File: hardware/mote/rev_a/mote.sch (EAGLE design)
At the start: 139 parts, among them J1 TC2030-JLINK-L, J2 TC2030-JLINK-NL, Q1 CSD22206W, Q10 CSD22206W, Q11 CSD22206W, Q2 CSD22206W, Q6 CSD22206W, Q7 CSD22206W, Q8 CSD22206W, Q9 CSD22206W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

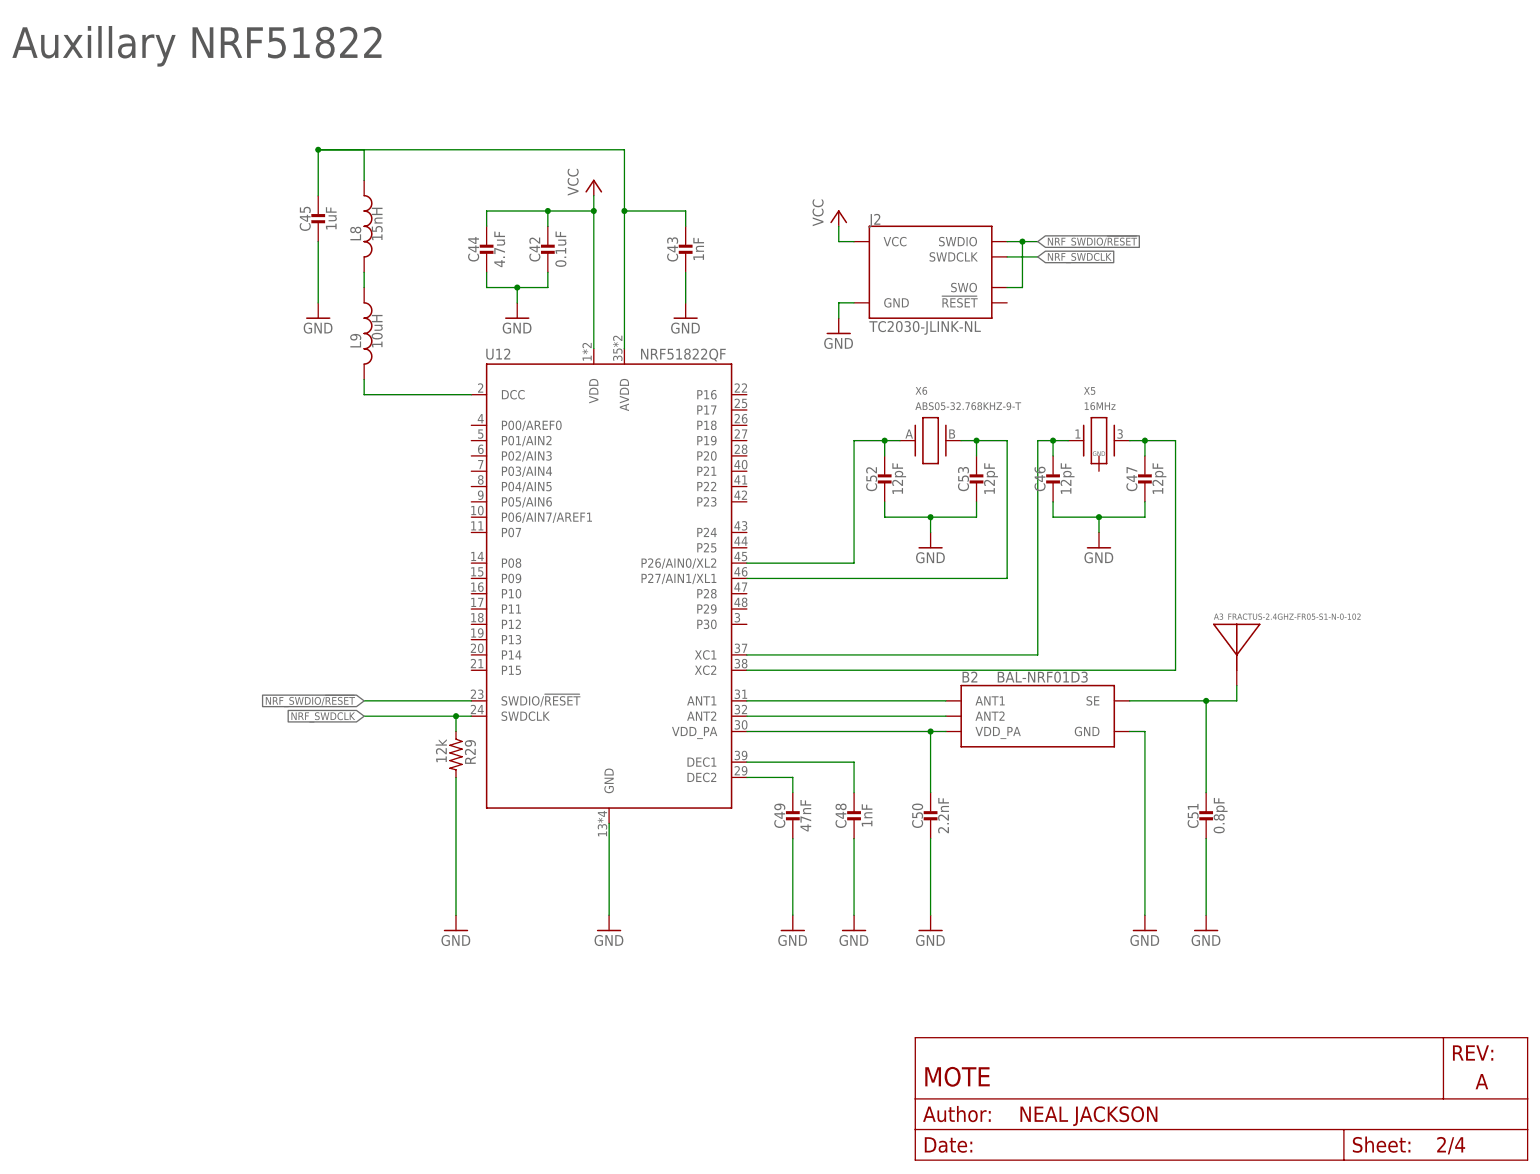
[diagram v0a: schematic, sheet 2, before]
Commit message: Connect up nrf51822, wire up sensors
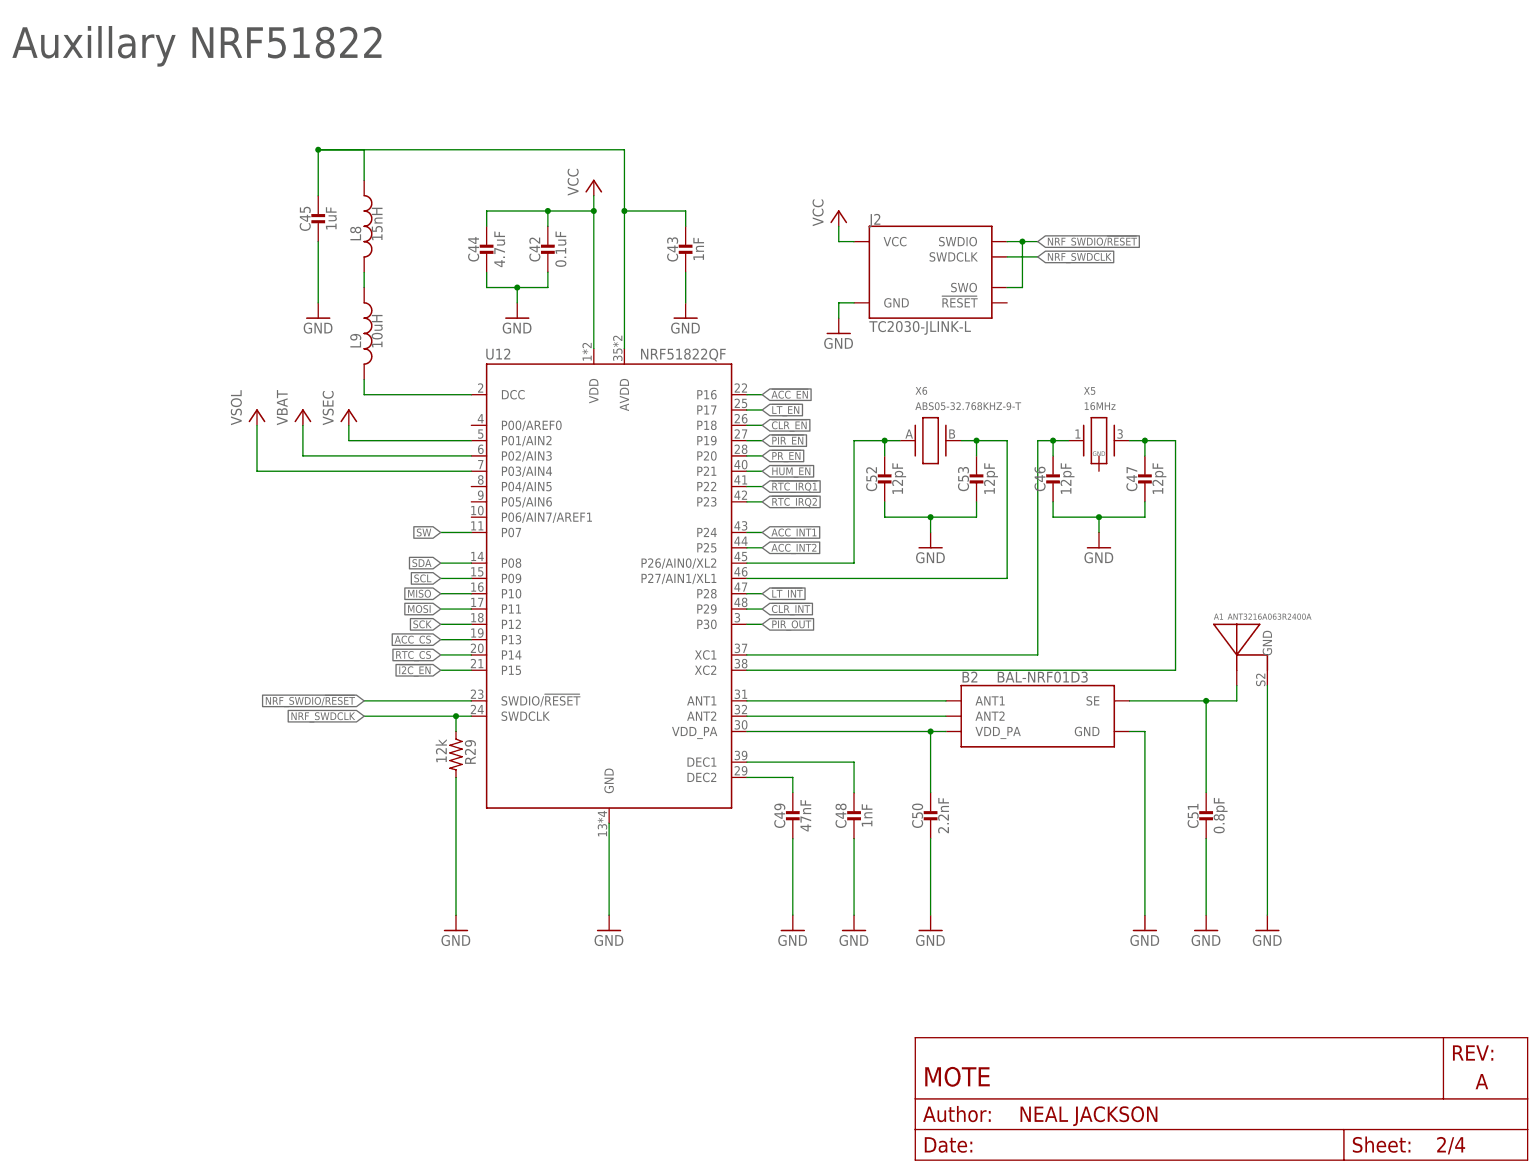
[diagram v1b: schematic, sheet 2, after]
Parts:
- removed A3: FRACTUS-2.4GHZ-FR05-S1-N-0-102, chips:FRACTUS-2.4GHZ-FR05-S1-N-0-102
- added A2: ANT3216A063R2400A, chips:ANT3216A063R2400A
- A1: value FRACTUS-2.4GHZ-FR05-S1-N-0-102 -> ANT3216A063R2400A; device chips:FRACTUS-2.4GHZ-FR05-S1-N-0-102 -> chips:ANT3216A063R2400A
- J2: value TC2030-JLINK-NL -> TC2030-JLINK-L; device connector:TC2030-JLINK-NL -> connector:TC2030-JLINK-L
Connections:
- removed net N$38: C28.1, D1.V+, L2.2, R22.2, TP1.TESTPOINT, U11.VIN
- new net VSOL: C28.1, D1.V+, L2.2, R22.2, TP1.TESTPOINT, U1.P0.29/AIN5, U11.VIN, U12.P03/AIN4
- net !ACC_EN: now also U12.P16
- net !CLR_EN: now also U12.P18
- net !CLR_INT: now also U12.P29
- net !HUM_EN: now also U12.P21
- net !I2C_EN: now also U12.P15
- net !LT_EN: now also U12.P17
- net !LT_INT: now also U12.P28
- net !PIR_EN: now also U12.P19
- net !PR_EN: now also U12.P20
- net !RTC_IRQ1: now also U12.P22
- net !RTC_IRQ2: now also U12.P23
- net ACC_CS: now also U12.P13
- net ACC_INT1: now also U12.P24
- net ACC_INT2: now also U12.P25
- net GND: now also A1.GND, A2.GND
- net MISO: now also U12.P10
- net MOSI: now also U12.P11
- net N$6: now also A2.ANTENNA; no longer A1.ANTENNA
- net N$62: now also A1.ANTENNA; no longer A3.ANTENNA
- net PIR_OUT: now also U12.P30
- net RTC_CS: now also U12.P14
- net SCK: now also U12.P12
- net SCL: now also U12.P09
- net SDA: now also U12.P08
- net SW: now also U12.P07; no longer U1.P0.04/AIN2
- net VBAT: now also U1.P0.04/AIN2, U12.P02/AIN3; no longer U1.P0.29/AIN5
- net VSEC: now also U12.P01/AIN2
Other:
- moved on the sheet: TP1

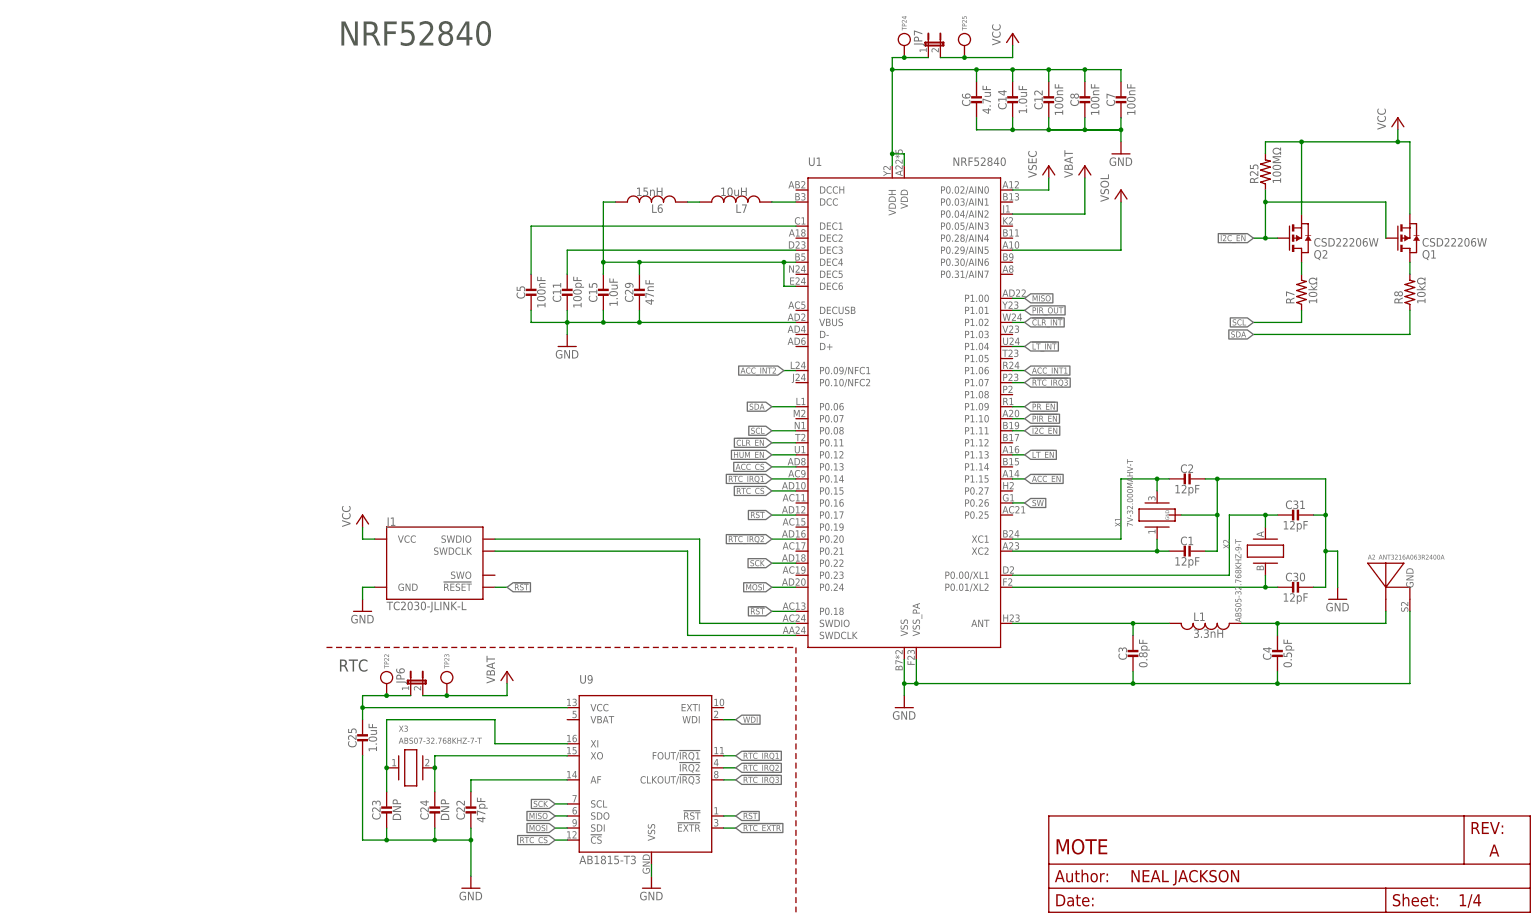
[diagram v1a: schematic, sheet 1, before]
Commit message: Rearrange sensors, current measurement
Ready for signal routing!
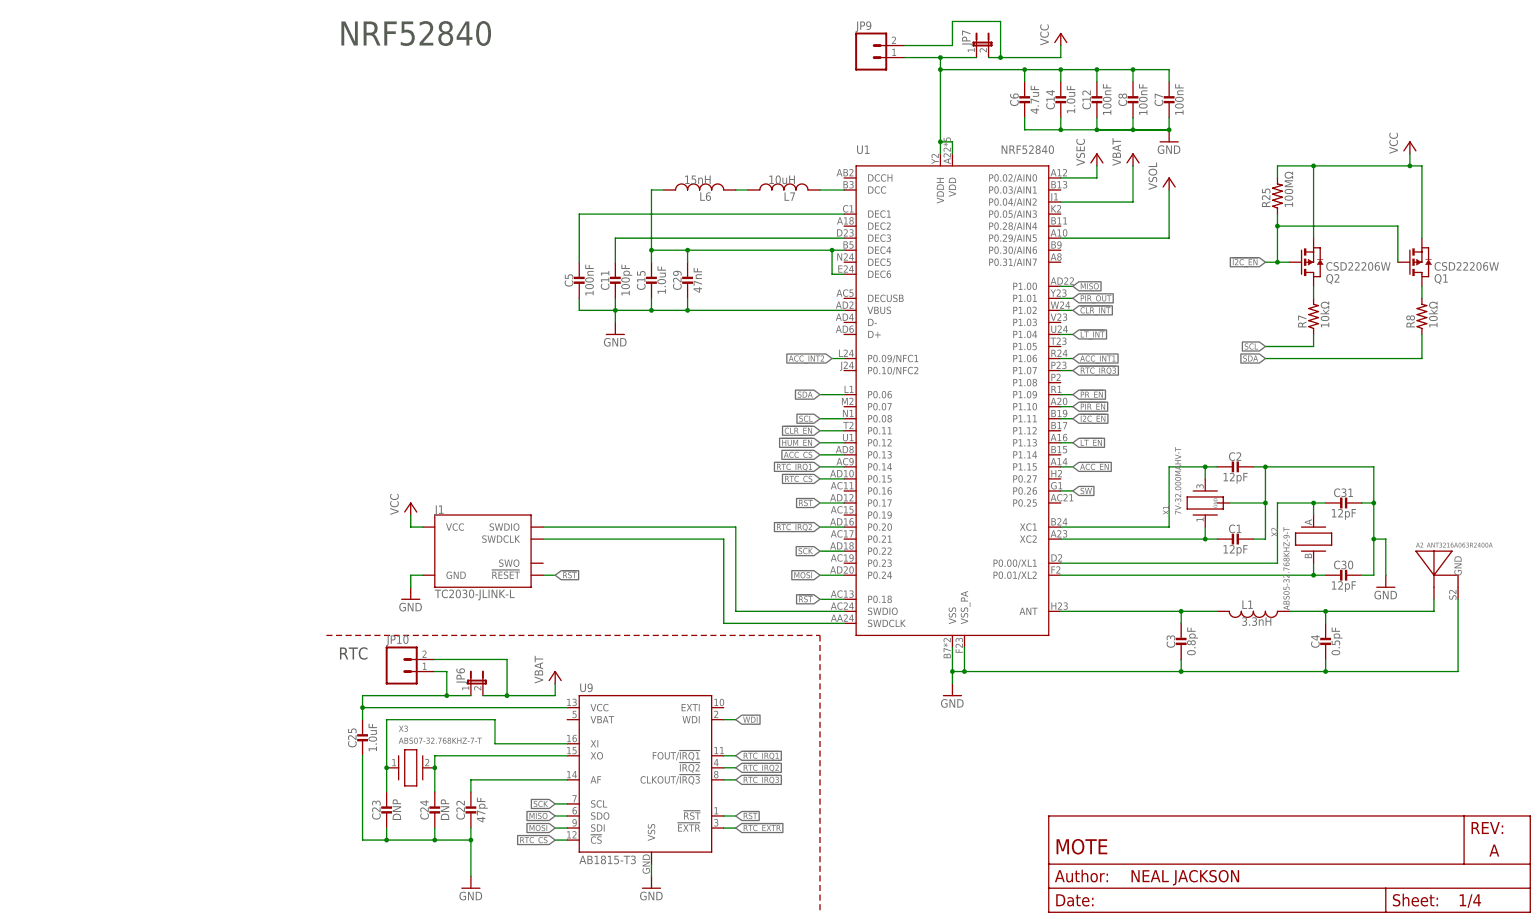
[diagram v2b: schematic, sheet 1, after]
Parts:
- removed BAT1: LTOHTC1020, batteries:LTOHTC1020
- removed TP12, TP13, TP14, TP15, TP16, TP17, TP18, TP19, TP20, TP21, TP22, TP23, TP24, TP25, TP28, TP29: TEST_POINT_0.040IN, headers:TEST_POINT_0.040IN
- added BT4: BAT_PACKCR123A, batteries:BAT_PACKCR123A
- added H1, H2, H3, H4: MOUNT-PAD-ROUND3.0, holes:MOUNT-PAD-ROUND3.0
- added JP10, JP11, JP12, JP13, JP14, JP15, JP16, JP9: (no value), SparkFun-Connectors:M02PTH
- BT1: value BAT_PACK2/3AA -> LTOHTC1020; device batteries:BAT_PACK2/3AA -> batteries:LTOHTC1020
- BT2: value BAT_PACKAA -> BAT_PACK2/3AA; device batteries:BAT_PACKAA -> batteries:BAT_PACK2/3AA
- BT3: value BAT_PACKCR123A -> BAT_PACKAA; device batteries:BAT_PACKCR123A -> batteries:BAT_PACKAA
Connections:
- removed net N$39: C12.1, C14.1, C6.1, C7.1, C8.1, JP7.1, TP24.TESTPOINT, U1.VDD, U1.VDDH
- removed net NRF_VCC: C42.1, C44.1, J2.VCC, U12.VDD
- new net VCC_JUMP: C12.1, C14.1, C42.1, C44.1, C6.1, C7.1, C8.1, JP7.1, JP9.1, U1.VDD, U1.VDDH, U12.VDD
- net GND: now also BT4.-, H1.MOUNT, H2.MOUNT, H3.MOUNT, H4.MOUNT; no longer BAT1.-
- net N$19: now also JP15.1; no longer TP18.TESTPOINT
- net N$24: now also JP14.1; no longer TP28.TESTPOINT
- net N$33: now also JP12.1; no longer TP14.TESTPOINT
- net N$36: now also JP16.1; no longer TP20.TESTPOINT
- net N$37: now also JP13.1; no longer TP16.TESTPOINT
- net N$40: now also JP11.1; no longer TP12.TESTPOINT
- net N$42: now also JP10.1; no longer TP22.TESTPOINT
- net VBAT: now also BT4.+, JP10.2; no longer BT1.+, TP23.TESTPOINT
- net VCC: now also J2.VCC, JP11.2, JP12.2, JP13.2, JP14.2, JP15.2, JP16.2, JP9.2; no longer TP13.TESTPOINT, TP15.TESTPOINT, TP17.TESTPOINT, TP19.TESTPOINT, TP21.TESTPOINT, TP25.TESTPOINT, TP29.TESTPOINT
- net VSEC: now also BT1.+; no longer BAT1.+
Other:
- note added: "Mounting Holes"
- moved on the sheet: A2, BT1, BT2, BT3, C1, C11, C12, C14, C15, C18, C19, C2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

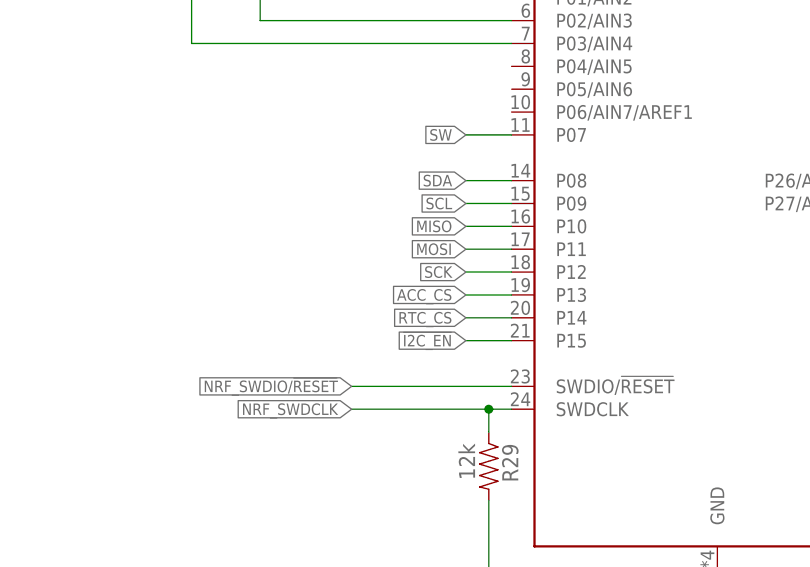
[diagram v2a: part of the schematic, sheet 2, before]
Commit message: Route I2C, sensor power pins
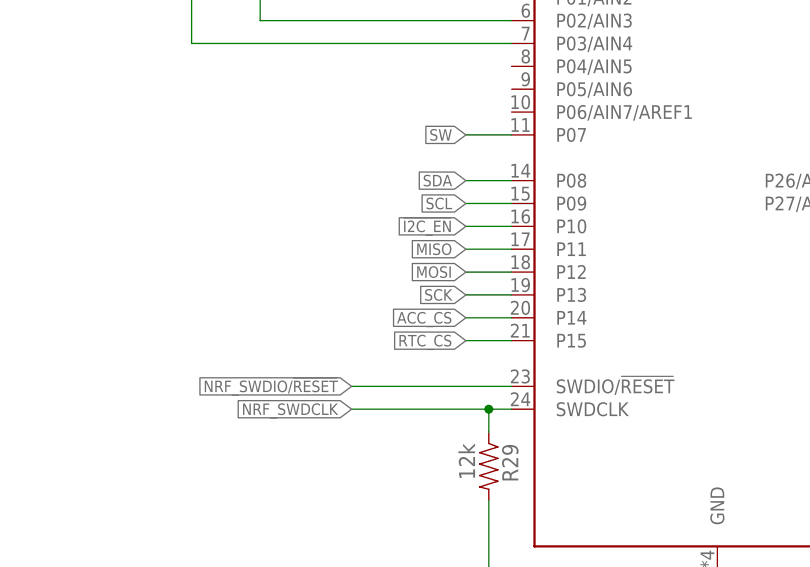
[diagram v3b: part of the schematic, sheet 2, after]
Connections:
- net !I2C_EN: now also U1.P1.09, U12.P10; no longer U1.P1.11, U12.P15
- net !PR_EN: now also U1.P1.11; no longer U1.P1.09
- net ACC_CS: now also U12.P14; no longer U12.P13
- net MISO: now also U12.P11; no longer U12.P10
- net MOSI: now also U12.P12; no longer U12.P11
- net RTC_CS: now also U12.P15; no longer U12.P14
- net SCK: now also U12.P13; no longer U12.P12
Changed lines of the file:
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@@
-</segment>
-</net>
-<net name="!PR_EN" class="0">
-<segment>
-<pinref part="U1" gate="G$1" pin="P1.09"/>
-<wire x1="154.94" y1="109.22" x2="157.48" y2="109.22" width="0.1524" layer="91"/>
-<label x="157.48" y="109.22" size="1.27" layer="95" xref="yes"/>
 </segment>
 </net>
@@
 </segment>
 <segment>
-<pinref part="U1" gate="G$1" pin="P1.11"/>
-<wire x1="154.94" y1="104.14" x2="157.48" y2="104.14" width="0.1524" layer="91"/>
-<label x="157.48" y="104.14" size="1.27" layer="95" xref="yes"/>
+<pinref part="U1" gate="G$1" pin="P1.09"/>
+<wire x1="154.94" y1="109.22" x2="157.48" y2="109.22" width="0.1524" layer="91"/>
+<label x="157.48" y="109.22" size="1.27" layer="95" xref="yes"/>
 </segment>
 </net>
@@
 <wire x1="154.94" y1="142.24" x2="177.8" y2="142.24" width="0.1524" layer="91"/>
 <wire x1="177.8" y1="142.24" x2="177.8" y2="152.4" width="0.1524" layer="91"/>
+</segment>
+</net>
+<net name="!PR_EN" class="0">
+<segment>
+<pinref part="U1" gate="G$1" pin="P1.11"/>
+<wire x1="154.94" y1="104.14" x2="157.48" y2="104.14" width="0.1524" layer="91"/>
+<label x="157.48" y="104.14" size="1.27" layer="95" xref="yes"/>
 </segment>
 </net>
@@
 <net name="MISO" class="0">
 <segment>
-<pinref part="U12" gate="G$1" pin="P10"/>
-<wire x1="78.74" y1="93.98" x2="73.66" y2="93.98" width="0.1524" layer="91"/>
-<label x="73.66" y="93.98" size="1.27" layer="95" rot="R180" xref="yes"/>
-</segment>
-</net>
-<net name="MOSI" class="0">
-<segment>
+<label x="73.66" y="91.44" size="1.27" layer="95" rot="R180" xref="yes"/>
 <pinref part="U12" gate="G$1" pin="P11"/>
 <wire x1="78.74" y1="91.44" x2="73.66" y2="91.44" width="0.1524" layer="91"/>
-<label x="73.66" y="91.44" size="1.27" layer="95" rot="R180" xref="yes"/>
-</segment>
-</net>
-<net name="SCK" class="0">
-<segment>
+</segment>
+</net>
+<net name="MOSI" class="0">
+<segment>
+<label x="73.66" y="88.9" size="1.27" layer="95" rot="R180" xref="yes"/>
 <pinref part="U12" gate="G$1" pin="P12"/>
 <wire x1="78.74" y1="88.9" x2="73.66" y2="88.9" width="0.1524" layer="91"/>
-<label x="73.66" y="88.9" size="1.27" layer="95" rot="R180" xref="yes"/>
-</segment>
-</net>
-<net name="ACC_CS" class="0">
-<segment>
+</segment>
+</net>
+<net name="SCK" class="0">
+<segment>
+<label x="73.66" y="86.36" size="1.27" layer="95" rot="R180" xref="yes"/>
 <pinref part="U12" gate="G$1" pin="P13"/>
 <wire x1="78.74" y1="86.36" x2="73.66" y2="86.36" width="0.1524" layer="91"/>
-<label x="73.66" y="86.36" size="1.27" layer="95" rot="R180" xref="yes"/>
-</segment>
-</net>
-<net name="RTC_CS" class="0">
-<segment>
+</segment>
+</net>
+<net name="ACC_CS" class="0">
+<segment>
+<label x="73.66" y="83.82" size="1.27" layer="95" rot="R180" xref="yes"/>
 <pinref part="U12" gate="G$1" pin="P14"/>
 <wire x1="78.74" y1="83.82" x2="73.66" y2="83.82" width="0.1524" layer="91"/>
-<label x="73.66" y="83.82" size="1.27" layer="95" rot="R180" xref="yes"/>
+</segment>
+</net>
+<net name="RTC_CS" class="0">
+<segment>
+<label x="73.66" y="81.28" size="1.27" layer="95" rot="R180" xref="yes"/>
+<pinref part="U12" gate="G$1" pin="P15"/>
+<wire x1="78.74" y1="81.28" x2="73.66" y2="81.28" width="0.1524" layer="91"/>
 </segment>
 </net>
@@
 <net name="!I2C_EN" class="0">
 <segment>
-<pinref part="U12" gate="G$1" pin="P15"/>
-<wire x1="78.74" y1="81.28" x2="73.66" y2="81.28" width="0.1524" layer="91"/>
-<label x="73.66" y="81.28" size="1.27" layer="95" rot="R180" xref="yes"/>
-</segment>
-</net>
+<label x="73.66" y="93.98" size="1.27" layer="95" rot="R180" xref="yes"/>
+<pinref part="U12" gate="G$1" pin="P10"/>
+<wire x1="78.74" y1="93.98" x2="73.66" y2="93.98" width="0.1524" layer="91"/>
+</segment>
+</net>
